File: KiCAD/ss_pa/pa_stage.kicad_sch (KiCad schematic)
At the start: 31 parts, among them J1 Conn_Coaxial_Small, J2 Screw_Terminal_01x02, J3 Conn_Coaxial_Small, J4 Conn_Coaxial_Small, Q3 IRF510, Q4 IRF510, T1 Transformer_1P_1S, T2 Transformer_1P_1S

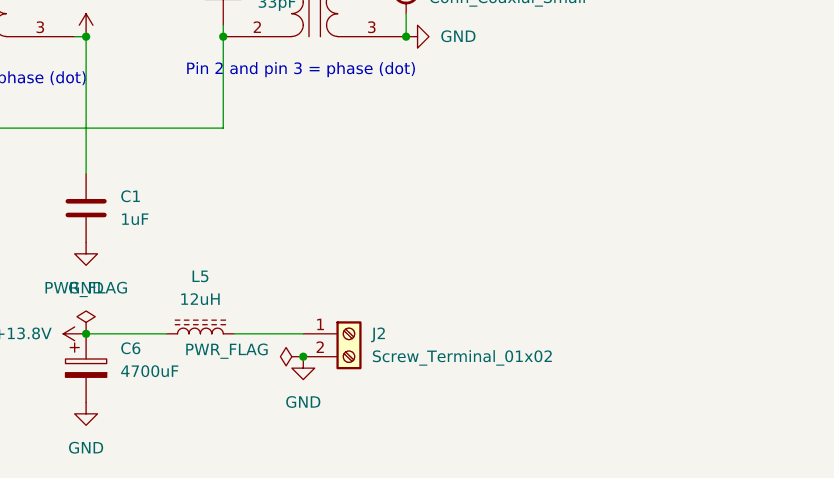
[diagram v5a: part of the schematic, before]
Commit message: KiCad revC: heartbeat-triggered SS PA power disconnect + flyback diodes
analog/power.kicad_sch:
- Added K6 (RLP20-12L10MS2F SPST-NO relay, 10A @ 30V DC contacts,
  12V/20mA coil) in series between +13.8V shack supply and J33
  (new 2-pin screw terminal supplying ss_pa board)
- K6 coil driven by existing Q5+Q7 series safety cascade on
  SS_PWR_RLY net: both Q5 (firmware control via PCF8575 P14) AND
  Q7 (CD14538B heartbeat watchdog Q_A) must be ON for the relay
  to energize. Firmware disable or heartbeat failure cuts PA power.
- Added 90R series resistor in the coil leg to drop +13.8V rail
  down to the 12V coil's nominal operating voltage
- Added D4 (1N4001 flyback diode) across K6 coil, cathode on +13.8V
  side, anode on SS_PWR_RLY (Q5 drain) side
- J7 (tube-era HV primary screw terminal) remains on the SS_PWR_RLY
  net so a future external tube-PA HV relay would share the same
  safety chain

ss_pa/pa_stage.kicad_sch:
- Added D2 (1N5822 Schottky, 3A/40V) flyback diode across L5. When
  the heartbeat relay opens with current flowing through L5, the
  12 uH inductor's stored energy (up to ~13 uJ at 1.5A) would
  otherwise swing the relay-side node hundreds of volts negative
  and arc the K6 contacts. D2 clamps that swing to ~V_f below the
  C6-held +13.8V bus.
- D2 polarity: cathode (pin 1) on J2/relay side, anode (pin 2) on
  +13.8V bus side.

Both netlists re-exported.

Co-Authored-By: Claude Opus 4.7 <noreply@anthropic.com>
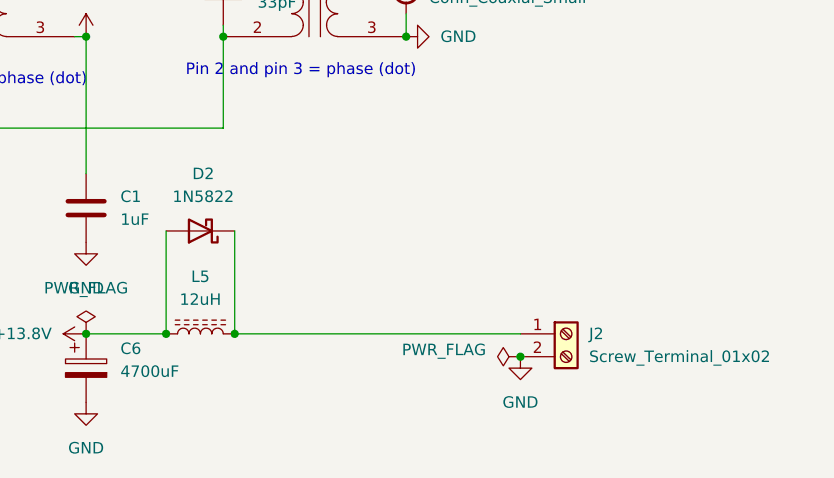
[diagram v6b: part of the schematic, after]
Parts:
- added D2: 1N5822, Diode_THT:D_DO-201AD_P15.24mm_Horizontal, symbol Diode:1N5822
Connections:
- net +13.8V: now also D2.2 (A)
- net at J2.1 (Pin_1), L5.2: now also D2.1 (K)
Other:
- moved on the sheet: J2
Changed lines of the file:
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@@
 	)
 	(junction
+		(at 218.44 128.27)
+		(diameter 0)
+		(color 0 0 0 0)
+	)
+	(junction
+		(at 226.06 128.27)
+		(diameter 0)
+		(color 0 0 0 0)
+	)
+	(junction
 		(at 161.29 92.71)
 		(diameter 0)
@@
 	)
 	(junction
-		(at 233.68 130.81)
+		(at 257.81 130.81)
 		(diameter 0)
 		(color 0 0 0 0)
@@
 	(wire
 		(pts
-			(xy 226.06 128.27) (xy 233.68 128.27)
+			(xy 153.67 60.96) (xy 153.67 57.15)
 		)
 		(stroke
@@
 	(wire
 		(pts
-			(xy 153.67 60.96) (xy 153.67 57.15)
+			(xy 245.11 85.09) (xy 245.11 87.63)
 		)
 		(stroke
@@
 	(wire
 		(pts
-			(xy 245.11 85.09) (xy 245.11 87.63)
+			(xy 115.57 88.9) (xy 118.11 88.9)
 		)
 		(stroke
@@
 	(wire
 		(pts
-			(xy 115.57 88.9) (xy 118.11 88.9)
+			(xy 161.29 80.01) (xy 161.29 82.55)
 		)
 		(stroke
@@
 	(wire
 		(pts
-			(xy 161.29 80.01) (xy 161.29 82.55)
+			(xy 218.44 116.84) (xy 218.44 128.27)
 		)
 		(stroke
@@
 	(wire
 		(pts
+			(xy 226.06 116.84) (xy 226.06 128.27)
+		)
+		(stroke
+			(width 0)
+			(type default)
+		)
+	)
+	(wire
+		(pts
 			(xy 161.29 114.3) (xy 161.29 119.38)
 		)
@@
 	(wire
 		(pts
+			(xy 226.06 128.27) (xy 257.81 128.27)
+		)
+		(stroke
+			(width 0)
+			(type default)
+		)
+	)
+	(wire
+		(pts
 			(xy 161.29 90.17) (xy 161.29 92.71)
 		)
@@
 	(symbol
 		(lib_id "power:PWR_FLAG")
-		(at 233.68 130.81 90)
+		(at 257.81 130.81 90)
 		(unit 1)
 		(body_style 1)
@@
 		(dnp no)
 		(property "Reference" "#FLG02"
-			(at 231.775 130.81 0)
+			(at 255.905 130.81 0)
 			(hide yes)
 			(show_name no)
@@
 		)
 		(property "Value" "PWR_FLAG"
-			(at 229.87 130.048 90)
+			(at 254 130.048 90)
 			(show_name no)
 			(do_not_autoplace no)
@@
 		)
 		(property "Footprint" ""
-			(at 233.68 130.81 0)
+			(at 257.81 130.81 0)
 			(hide yes)
 			(show_name no)
@@
 		)
 		(property "Datasheet" ""
-			(at 233.68 130.81 0)
+			(at 257.81 130.81 0)
 			(hide yes)
 			(show_name no)
@@
 		)
 		(property "Description" "Special symbol for telling ERC where power comes from"
-			(at 233.68 130.81 0)
+			(at 257.81 130.81 0)
 			(hide yes)
 			(show_name no)
@@
 	(symbol
 		(lib_id "power:GND")
-		(at 233.68 130.81 0)
+		(at 257.81 130.81 0)
 		(unit 1)
 		(body_style 1)
@@
 		(fields_autoplaced yes)
 		(property "Reference" "#PWR07"
-			(at 233.68 137.16 0)
+			(at 257.81 137.16 0)
 			(hide yes)
 			(show_name no)
@@
 		)
 		(property "Value" "GND"
-			(at 233.68 135.89 0)
+			(at 257.81 135.89 0)
 			(show_name no)
 			(do_not_autoplace no)
@@
 		)
 		(property "Footprint" ""
-			(at 233.68 130.81 0)
+			(at 257.81 130.81 0)
 			(hide yes)
 			(show_name no)
@@
 		)
 		(property "Datasheet" ""
-			(at 233.68 130.81 0)
+			(at 257.81 130.81 0)
 			(hide yes)
 			(show_name no)
@@
 		)
 		(property "Description" "Power symbol creates a global label with name \"GND\" , ground"
-			(at 233.68 130.81 0)
+			(at 257.81 130.81 0)
 			(hide yes)
 			(show_name no)
@@
 	(symbol
 		(lib_id "Connector:Screw_Terminal_01x02")
-		(at 238.76 128.27 0)
+		(at 262.89 128.27 0)
 		(unit 1)
 		(body_style 1)
@@
 		(fields_autoplaced yes)
 		(property "Reference" "J2"
-			(at 241.3 128.2699 0)
+			(at 265.43 128.2699 0)
 			(show_name no)
 			(do_not_autoplace no)
@@
 		)
 		(property "Value" "Screw_Terminal_01x02"
-			(at 241.3 130.8099 0)
+			(at 265.43 130.8099 0)
 			(show_name no)
 			(do_not_autoplace no)
@@
 		)
 		(property "Footprint" ""
-			(at 238.76 128.27 0)
+			(at 262.89 128.27 0)
 			(hide yes)
 			(show_name no)
@@
 		)
 		(property "Datasheet" ""
-			(at 238.76 128.27 0)
+			(at 262.89 128.27 0)
 			(hide yes)
 			(show_name no)
@@
 		)
 		(property "Description" "Generic screw terminal, single row, 01x02, script generated (kicad-library-utils/schlib/autogen/connector/)"
-			(at 238.76 128.27 0)
+			(at 262.89 128.27 0)
 			(hide yes)
 			(show_name no)
@@
 					(unit 1)
 				)
+			)
+		)
+	)
+	(symbol
+		(lib_id "Diode:1N5822")
+		(at 222.25 116.84 180)
+		(unit 1)
+		(body_style 1)
+		(exclude_from_sim no)
+		(in_bom yes)
+		(on_board yes)
+		(in_pos_files yes)
+		(dnp no)
+		(fields_autoplaced yes)
+		(property "Reference" "D2"
+			(at 222.5675 110.49 0)
+			(show_name no)
+			(do_not_autoplace no)
+			(effects
+				(font
+					(size 1.27 1.27)
+				)
+			)
+		)
+		(property "Value" "1N5822"
+			(at 222.5675 113.03 0)
+			(show_name no)
+			(do_not_autoplace no)
+			(effects
+				(font
+					(size 1.27 1.27)
+				)
+			)
+		)
+		(property "Footprint" "Diode_THT:D_DO-201AD_P15.24mm_Horizontal"
+			(at 222.25 112.395 0)
+			(hide yes)
+			(show_name no)
+			(do_not_autoplace no)
+			(effects
+				(font
+					(size 1.27 1.27)
+				)
+			)
+		)
+		(property "Datasheet" "http://www.vishay.com/docs/88526/1n5820.pdf"
+			(at 222.25 116.84 0)
+			(hide yes)
+			(show_name no)
+			(do_not_autoplace no)
+			(effects
+				(font
+					(size 1.27 1.27)
+				)
+			)
+		)
+		(property "Description" "40V 3A Schottky Barrier Rectifier Diode, DO-201AD"
+			(at 222.25 116.84 0)
+			(hide yes)
+			(show_name no)
+			(do_not_autoplace no)
+			(effects
+				(font
+					(size 1.27 1.27)
+				)
+			)
+		)
+		(pin "1"
+		)
+		(pin "2"
+		)
+		(instances
+			(project "ss_pa"
+				(path "/7b9fe991-54d6-43c4-a637-0ed9ee982c42/6995ca2b-35a4-4871-8cf2-3a0067e62105"
+					(reference "D2")
+					(unit 1)
+				)

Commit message: revC: accumulated schematic/netlist updates + BOM tooling
- analog + ss_pa netlists regenerated to current schematic state
- interface/arduino/dac/power sheet updates on analog
- fault_shutdown and pa_stage edits on ss_pa (footprint assignments)
- assign_cap_footprints.py: additional VALUE_TO_FOOTPRINT entries
- gen_board_boms.py: per-board BOM generator (multi-sheet .xlsx by
  component category, first-match-wins bucketing, DNP exclusion)
- gen_total_bom.py: consolidated BOM across analog + frontpanel + ss_pa
  for a single Mouser order, board-prefixed references, mixed-footprint
  flagging per Value row

Co-Authored-By: Claude Opus 4.7 <noreply@anthropic.com>
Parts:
- C1, C2: footprint (none) -> Capacitor_THT:C_Rect_L7.2mm_W4.5mm_P5.00mm
- C10, C3, C4, C5, C7, C8, C9: footprint (none) -> Capacitor_THT:C_Disc_D5.0mm_W2.5mm_P5.00mm
- C6: footprint (none) -> xmitter:CP_Radial_Kemet_ESK_D22.0mm_P10.00mm
- J1, J3, J4: footprint (none) -> xmitter:SMA_Cinch_142-0701-201_Vertical_JackPCB
- J2: footprint (none) -> TerminalBlock_Phoenix:TerminalBlock_Phoenix_MKDS-1,5-2_1x02_P5.00mm_Horizontal
- L1, L2, L3, L4: footprint (none) -> Inductor_THT:L_Axial_L5.3mm_D2.2mm_P2.54mm_Vertical
- L5: footprint (none) -> xmitter:T50-6_Flat_HandWound
- R1, R2, R3, R4, R5, R6, R7, R8: footprint (none) -> Resistor_THT:R_Axial_DIN0207_L6.3mm_D2.5mm_P10.16mm_Horizontal
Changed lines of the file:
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@@
 			)
 		)
-		(property "Footprint" ""
+		(property "Footprint" "Inductor_THT:L_Axial_L5.3mm_D2.2mm_P2.54mm_Vertical"
 			(at 153.67 64.77 0)
 			(hide yes)
@@
 			)
 		)
-		(property "Footprint" ""
+		(property "Footprint" "Resistor_THT:R_Axial_DIN0207_L6.3mm_D2.5mm_P10.16mm_Horizontal"
 			(at 157.734 58.166 90)
 			(hide yes)
@@
 			)
 		)
-		(property "Footprint" ""
+		(property "Footprint" "xmitter:T50-6_Flat_HandWound"
 			(at 222.25 128.27 0)
 			(hide yes)
@@
 			)
 		)
-		(property "Footprint" ""
+		(property "Footprint" "Resistor_THT:R_Axial_DIN0207_L6.3mm_D2.5mm_P10.16mm_Horizontal"
 			(at 158.496 96.774 90)
 			(hide yes)
@@
 			)
 		)
-		(property "Footprint" ""
+		(property "Footprint" "Capacitor_THT:C_Disc_D5.0mm_W2.5mm_P5.00mm"
 			(at 160.3248 119.38 0)
 			(hide yes)
@@
 			)
 		)
-		(property "Footprint" ""
+		(property "Footprint" "Capacitor_THT:C_Rect_L7.2mm_W4.5mm_P5.00mm"
 			(at 210.5152 118.11 0)
 			(hide yes)
@@
 			)
 		)
-		(property "Footprint" ""
+		(property "Footprint" "Inductor_THT:L_Axial_L5.3mm_D2.2mm_P2.54mm_Vertical"
 			(at 153.67 119.38 0)
 			(hide yes)
@@
 			)
 		)
-		(property "Footprint" ""
+		(property "Footprint" "xmitter:SMA_Cinch_142-0701-201_Vertical_JackPCB"
 			(at 245.11 90.17 0)
 			(hide yes)
@@
 			)
 		)
-		(property "Footprint" ""
+		(property "Footprint" "Resistor_THT:R_Axial_DIN0207_L6.3mm_D2.5mm_P10.16mm_Horizontal"
 			(at 162.306 96.774 90)
 			(hide yes)
@@
 			)
 		)
-		(property "Footprint" ""
+		(property "Footprint" "xmitter:SMA_Cinch_142-0701-201_Vertical_JackPCB"
 			(at 140.97 74.93 0)
 			(hide yes)
@@
 			)
 		)
-		(property "Footprint" ""
+		(property "Footprint" "Capacitor_THT:C_Disc_D5.0mm_W2.5mm_P5.00mm"
 			(at 126.6952 81.28 0)
 			(hide yes)
@@
 			)
 		)
-		(property "Footprint" ""
+		(property "Footprint" "Resistor_THT:R_Axial_DIN0207_L6.3mm_D2.5mm_P10.16mm_Horizontal"
 			(at 157.734 125.984 90)
 			(hide yes)
@@
 			)
 		)
-		(property "Footprint" ""
+		(property "Footprint" "Capacitor_THT:C_Rect_L7.2mm_W4.5mm_P5.00mm"
 			(at 188.9252 85.09 0)
 			(hide yes)
@@
 			)
 		)
-		(property "Footprint" ""
+		(property "Footprint" "Resistor_THT:R_Axial_DIN0207_L6.3mm_D2.5mm_P10.16mm_Horizontal"
 			(at 162.306 86.614 90)
 			(hide yes)
@@
 			)
 		)
-		(property "Footprint" ""
+		(property "Footprint" "Resistor_THT:R_Axial_DIN0207_L6.3mm_D2.5mm_P10.16mm_Horizontal"
 			(at 122.174 92.964 90)
 			(hide yes)
@@
 			)
 		)
-		(property "Footprint" ""
+		(property "Footprint" "Capacitor_THT:C_Disc_D5.0mm_W2.5mm_P5.00mm"
 			(at 126.6952 101.6 0)
 			(hide yes)
@@
 			)
 		)
-		(property "Footprint" ""
+		(property "Footprint" "Resistor_THT:R_Axial_DIN0207_L6.3mm_D2.5mm_P10.16mm_Horizontal"
 			(at 158.496 86.614 90)
 			(hide yes)
@@
 			)
 		)
-		(property "Footprint" ""
+		(property "Footprint" "Capacitor_THT:C_Disc_D5.0mm_W2.5mm_P5.00mm"
 			(at 225.7552 93.98 0)
 			(hide yes)
@@
 			)
 		)
-		(property "Footprint" ""
+		(property "Footprint" "xmitter:CP_Radial_Kemet_ESK_D22.0mm_P10.00mm"
 			(at 210.5152 135.89 0)
 			(hide yes)
@@
 			)
 		)
-		(property "Footprint" ""
+		(property "Footprint" "Inductor_THT:L_Axial_L5.3mm_D2.2mm_P2.54mm_Vertical"
 			(at 129.54 93.98 0)
 			(hide yes)
@@
 			)
 		)
-		(property "Footprint" ""
+		(property "Footprint" "TerminalBlock_Phoenix:TerminalBlock_Phoenix_MKDS-1,5-2_1x02_P5.00mm_Horizontal"
 			(at 262.89 128.27 0)
 			(hide yes)
@@
 			)
 		)
-		(property "Footprint" ""
+		(property "Footprint" "Capacitor_THT:C_Disc_D5.0mm_W2.5mm_P5.00mm"
 			(at 151.13 73.9648 0)
 			(hide yes)
@@
 			)
 		)
-		(property "Footprint" ""
+		(property "Footprint" "xmitter:SMA_Cinch_142-0701-201_Vertical_JackPCB"
 			(at 140.97 109.22 0)
 			(hide yes)
@@
 			)
 		)
-		(property "Footprint" ""
+		(property "Footprint" "Resistor_THT:R_Axial_DIN0207_L6.3mm_D2.5mm_P10.16mm_Horizontal"
 			(at 122.174 89.916 90)
 			(hide yes)
@@
 			)
 		)
-		(property "Footprint" ""
+		(property "Footprint" "Capacitor_THT:C_Disc_D5.0mm_W2.5mm_P5.00mm"
 			(at 160.3248 64.77 0)
 			(hide yes)
@@
 			)
 		)
-		(property "Footprint" ""
+		(property "Footprint" "Capacitor_THT:C_Disc_D5.0mm_W2.5mm_P5.00mm"
 			(at 151.13 108.2548 0)
 			(hide yes)
@@
 			)
 		)
-		(property "Footprint" ""
+		(property "Footprint" "Inductor_THT:L_Axial_L5.3mm_D2.2mm_P2.54mm_Vertical"
 			(at 129.54 88.9 0)
 			(hide yes)

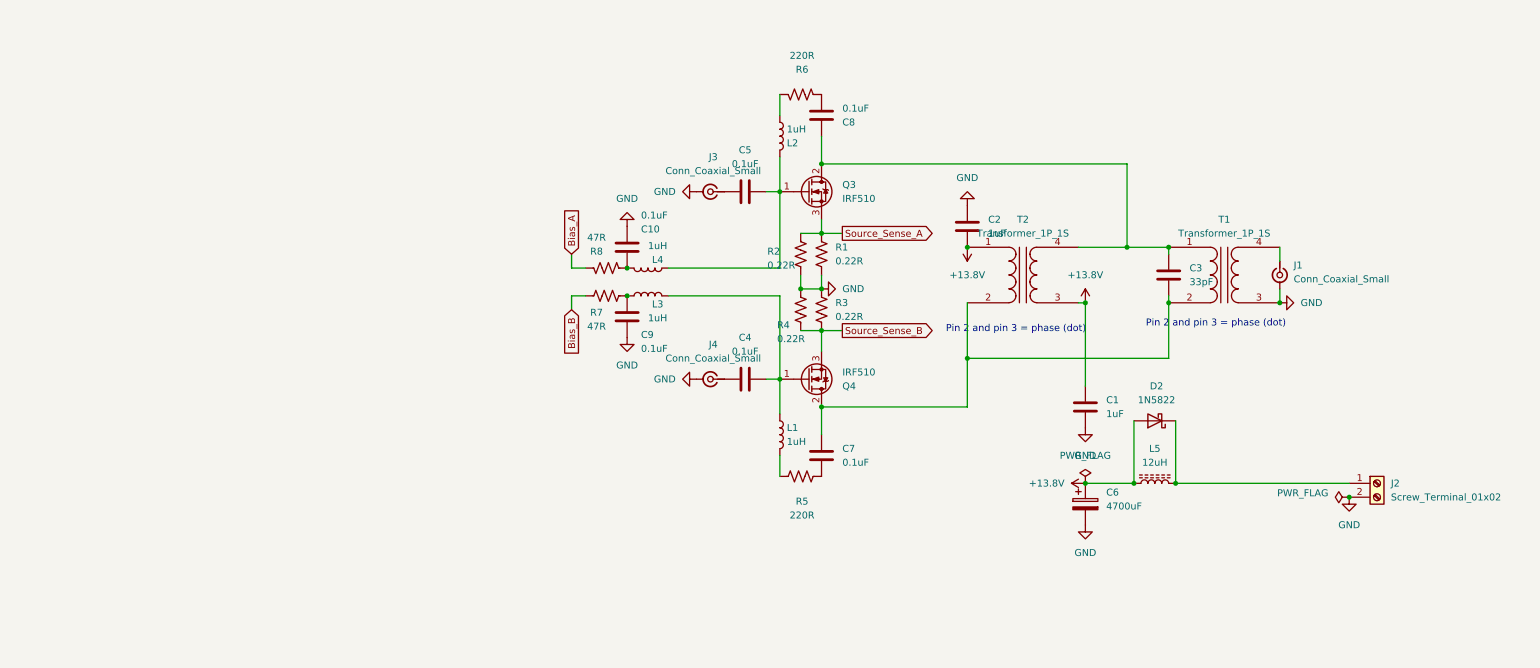
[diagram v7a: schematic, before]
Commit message: revD: DGFET-DAC bias scheme, kit-style xfmr naming, custom footprints, Output LPF project
Architecture refinements since the previous revD commit (f8d7058):

Analog board (vfo_complete, arduino, dac, power sheets):
  * MCP4922 (U4) ch B exposed as DRIVER_BIAS DAC output -> J31 pin 6
    (replaces the +3.3V pin that was on J31 pin 6 before). Analog's U4
    now controls the ss_pa BS170 driver DC bias point directly from
    firmware -- cleaner than the kit's trimmer+Q201 scheme.
  * MCP4728 (U3) ch A/B exposed as PA_Bias_A_Raw / PA_Bias_B_Raw ->
    J31 pins 7, 8. These feed the ss_pa CD74HC4066 fault-switch (U2),
    which gates them to PA_Bias_A/B on the IRF510 gates. On FAULT_N
    low, switch opens -> IRF510 bias collapses -> conduction cuts.
  * Rename pass: Bias_A/B/_Raw labels -> PA_Bias_A/B/_Raw everywhere
    (analog J3 screw-terminal, umbilical J31, ss_pa U2 inputs). Prefix
    disambiguates from DRIVER_BIAS which drives a different stage.
  * J2 (band-select RJ45 to Output LPF board): added RLY_40 provision.
    Pin layout reorganized -- RLY_40 lives at pin 5, pin 6 kept as a
    spare for a future 6th band.

ss_pa board (pa_stage, fault_shutdown, lpf sheets):
  * Driver + final BS170/IRF510 topology drawn following QRP Labs
    10W Linear kit (RF IN -> T201 input xfmr -> BS170 PP driver
    (Q2, Q6) -> T202 interstage -> IRF510 PP finals (Q3, Q4) ->
    T203 bifilar drain feed -> T204 output xfmr -> RF out).
  * Transformer references renamed to match the kit: T201 (input,
    BN61-2402), T202 (interstage, BN61-2402), T203 (drain feed,
    T50-43), T204 (output, BN43-202).
  * Driver bias filter on DRIVER_BIAS: C19 (0.1uF) + C20 (100pF)
    bulk + HF bypass, into T201 secondary CT (pin 4).
  * +3.3V now locally regulated on ss_pa (MCP1700x-330xxTO, U13)
    from +13.8V, powering U1 (LM393) and U2 (CD74HC4066). J31
    pin 6 freed up for DRIVER_BIAS.
  * Duplicate RJ45 J7 deleted (was a leftover from pre-DAC-bias era).
  * J3 (SMA RF input from analog) foo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
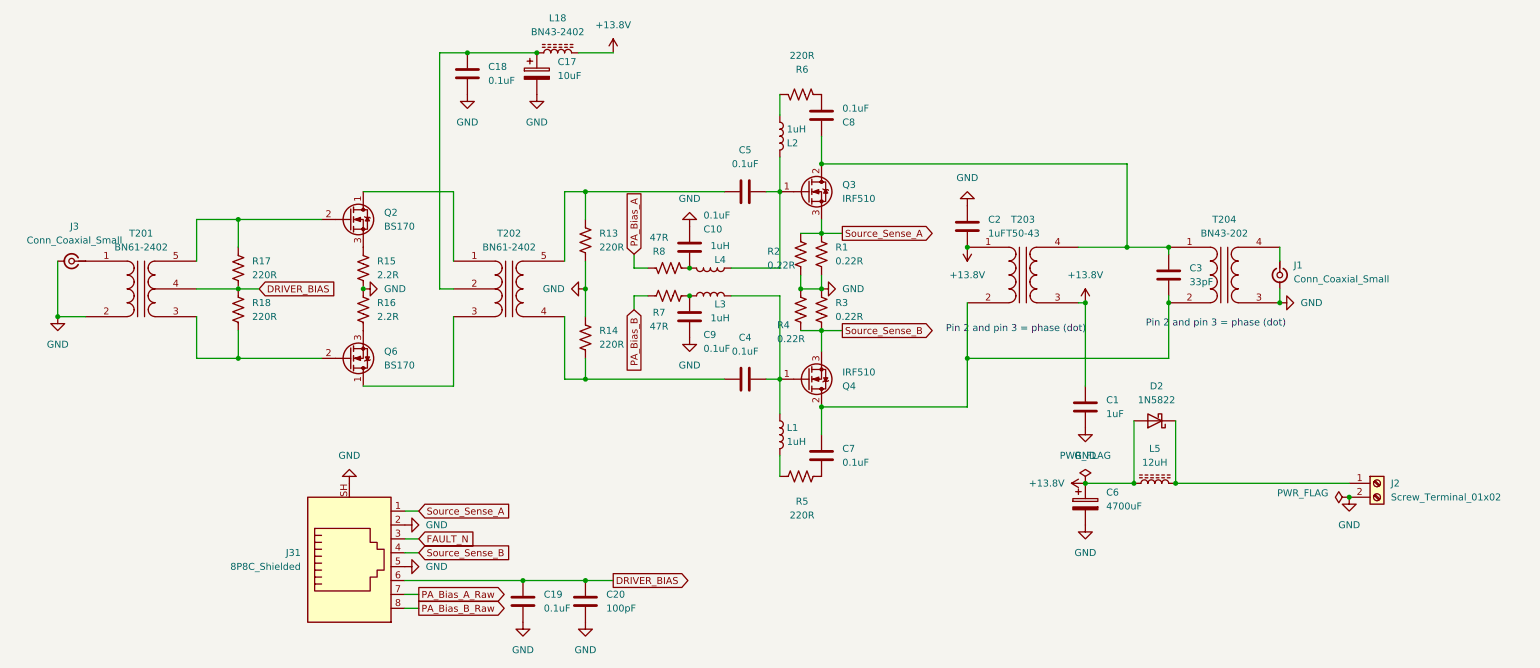
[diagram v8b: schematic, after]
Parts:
- removed J4: Conn_Coaxial_Small, xmitter:SMA_Cinch_142-0701-201_Vertical_JackPCB, symbol Connector:Conn_Coaxial_Small
- added C17: 10uF, Capacitor_THT:CP_Radial_D5.0mm_P2.00mm, symbol Device:C_Polarized
- added C18, C19: 0.1uF, Capacitor_THT:C_Disc_D5.0mm_W2.5mm_P5.00mm, symbol Device:C
- added C20: 100pF, Capacitor_THT:C_Rect_L7.0mm_W3.5mm_P5.00mm, symbol Device:C
- added J31: 8P8C_Shielded, xmitter:Amphenol_RJE1D-188_Horizontal_Shielded, symbol Connector:8P8C_Shielded
- added L18: BN43-2402, xmitter:BN43-2402_Vertical_HandWound, symbol Device:L_Ferrite
- added Q2, Q6: BS170, Package_TO_SOT_THT:TO-92_Inline, symbol Transistor_FET:BS170
- added R13, R14, R17, R18: 220R, Resistor_THT:R_Axial_DIN0207_L6.3mm_D2.5mm_P10.16mm_Horizontal, symbol Device:R_US
- added R15, R16: 2.2R, Resistor_THT:R_Axial_DIN0207_L6.3mm_D2.5mm_P10.16mm_Horizontal, symbol Device:R_US
- added T201: BN61-2402, xmitter:BN61-2402_Vertical_HandWound_SecondaryCT, symbol Device:Transformer_1P_SS
- added T202: BN61-2402, xmitter:BN61-2402_Vertical_HandWound_PrimaryCT, symbol Device:Transformer_SP_1S
- T203: renamed from T2; value Transformer_1P_1S -> T50-43; footprint (none) -> xmitter:T50-43_Vertical_Bifilar_HandWound
- T204: renamed from T1; value Transformer_1P_1S -> BN43-202; footprint (none) -> xmitter:BN43-202_Horizontal_HandWound
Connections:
- net +13.8V: now also L18.2
- net GND: now also C17.2, C18.2, C19.2, C20.2, J31.2, J31.5, J31.SH, R13.2, R14.1, R15.2, R16.1, T201.2 (AB)
- net Source_Sense_A: now also J31.1
- net Source_Sense_B: now also J31.4
- net at C5.1: now also R13.1, T202.5 (S2); no longer J3.1 (In)
- net at C4.1: now also R14.2, T202.4 (S1)
- net Bias_A renamed PA_Bias_A
- net Bias_B renamed PA_Bias_B
- new net: Q2.1 (D), T202.1 (PR1)
- new net: C17.1, C18.1, L18.1, T202.2 (PM)
- new net: Q6.1 (D), T202.3 (PR2)
- new net: Q2.3 (S), R15.1
- new net: Q6.2 (G), R18.2, T201.3 (SA)
- new net: Q6.3 (S), R16.2
- new net: Q2.2 (G), R17.1, T201.5 (SB)
- new net: J3.1 (In), T201.1 (AA)
- new net DRIVER_BIAS: C19.1, C20.1, J31.6, R17.2, R18.1, T201.4 (SC)
- new net FAULT_N: J31.3
- new net PA_Bias_A_Raw: J31.7
- new net PA_Bias_B_Raw: J31.8
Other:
- moved on the sheet: C10, C9, L3, L4, R7, R8
